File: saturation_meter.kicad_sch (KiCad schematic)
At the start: 18 parts, among them J1 DUT, Q1 Q_NMOS_GDS, Q2 Q_NMOS_GDS, U1 OP07, U2 IR2112

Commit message: Added cap
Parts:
- removed R4: 30k, symbol Device:R
- removed R5: 100k, symbol Device:R
- removed U1: OP07, symbol Amplifier_Operational:OP07
- added C10, C9: 100n, symbol Device:C
- added C11, C12, C13, C4: 4700u, symbol Device:C_Polarized_US
- added C5, C6, C7, C8: 1n, symbol Device:C
- added D4: D, symbol Device:D
- added J2: DUT, symbol Connector_Generic:Conn_01x02
- added R10: 1, symbol Device:R
- added R11, R8: 10k, symbol Device:R
- added R12, R9: 1k, symbol Device:R
- added U1: LM7812_TO220, Package_TO_SOT_THT:TO-220-3_Vertical, symbol Regulator_Linear:LM7812_TO220
- Q1, Q2: value Q_NMOS_GDS -> BUK556
- R2: value 100k -> 1k
- R3: value 30k -> 1k
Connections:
- net GND: now also R3.2, C10.2, C11.2, C12.2, C13.2, C4.2, C5.2, C6.2, C7.2, C8.2, C9.2, J2.1 (Pin_1), R12.1, R9.1, U1.2 (GND)
- net high_nmos_s: now also R8.2
- net low_nmos_g: now also R2.2; no longer R3.1
- net driver_ho: now reaches R6.1, U2.7 (HO)
- net driver_ho: now also R7.1
- net low_nmos_d: now reaches D2.2 (A), J1.2 (Pin_2), Q1.2 (D)
- net low_nmos_d: now also R11.2
- net driver_lo: now reaches U2.1 (LO)
- net driver_lo: no longer R7.1
- net +12V: now reaches C2.1, D3.2 (A), U2.3 (VCC)
- net +12V: now also C10.1, U1.3 (VO)
- net i_sense_high: now reaches R2.1
- net i_sense_high: now also C8.1; no longer R3.2
- net vbus: now reaches D2.1 (K), Q2.2 (D)
- net vbus: now also C11.1, C12.1, C13.1, C4.1, C9.1, R10.2, U1.1 (VI)
- new net: D4.1 (K), R10.1
- new net: D4.2 (A), J2.2 (Pin_2)
- new net dut_high: C5.1, R8.1, R9.2
- new net dut_low: C6.1, R11.1, R12.2
- new net i_sense_low: C7.1, R3.1
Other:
- moved on the sheet: C1, C2, C3, D1, D2, D3, J1, Q1, Q2, R1, R6, R7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

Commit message: Released 1.0.0 of schematic
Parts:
- removed C1, C10, C2: 100n, symbol Device:C
- removed D1, D2, D4: D, symbol Device:D
- removed U1: LM7812_TO220, Package_TO_SOT_THT:TO-220-3_Vertical, symbol Regulator_Linear:LM7812_TO220
- added C12, C13, C9: 2u2, Capacitor_THT:CP_Radial_D6.3mm_P2.50mm, symbol Device:C_Polarized_US
- added D1, D2, D3: 1N5822, Diode_THT:D_DO-201AD_P15.24mm_Horizontal, symbol Diode:1N5822
- added D5, D6: LED, LED_THT:LED_D5.0mm, symbol Device:LED
- added J3: Inputs, Connector_PinHeader_2.54mm:PinHeader_1x03_P2.54mm_Vertical, symbol Connector_Generic:Conn_01x03
- added J4: Outputs, Connector_PinHeader_2.54mm:PinHeader_1x04_P2.54mm_Vertical, symbol Connector_Generic:Conn_01x04
- added J5: UC, Connector_PinHeader_2.54mm:PinHeader_1x02_P2.54mm_Vertical, symbol Connector_Generic:Conn_01x02
- added Q3: BC328, Package_TO_SOT_THT:TO-92_Inline, symbol Transistor_BJT:BC328
- added R11, R14: 1k6, Resistor_SMD:R_1206_3216Metric_Pad1.30x1.75mm_HandSolder, symbol Device:R
- added R12, R17, R18, R19: 8k2, Resistor_SMD:R_1206_3216Metric_Pad1.30x1.75mm_HandSolder, symbol Device:R
- added R13, R15, R16: 100, Resistor_SMD:R_1206_3216Metric_Pad1.30x1.75mm_HandSolder, symbol Device:R
- added U1: LF33_TO220, Package_TO_SOT_THT:TO-220-3_Vertical, symbol Regulator_Linear:LF33_TO220
- C1: renamed from C4; footprint (none) -> Capacitor_THT:CP_Radial_D30.0mm_P10.00mm_SnapIn
- C10: renamed from C7; footprint (none) -> Capacitor_SMD:C_1206_3216Metric_Pad1.33x1.80mm_HandSolder
- C11: renamed from C3; footprint (none) -> Capacitor_SMD:C_1206_3216Metric_Pad1.33x1.80mm_HandSolder
- C2: renamed from C11; footprint (none) -> Capacitor_THT:CP_Radial_D30.0mm_P10.00mm_SnapIn
- C3: renamed from C12; footprint (none) -> Capacitor_THT:CP_Radial_D30.0mm_P10.00mm_SnapIn
- C4: renamed from C13; footprint (none) -> Capacitor_THT:CP_Radial_D30.0mm_P10.00mm_SnapIn
- C5: renamed from C6; footprint (none) -> Capacitor_SMD:C_1206_3216Metric_Pad1.33x1.80mm_HandSolder
- C6: renamed from C5; footprint (none) -> Capacitor_SMD:C_1206_3216Metric_Pad1.33x1.80mm_HandSolder
- C7: renamed from C8; footprint (none) -> Capacitor_SMD:C_1206_3216Metric_Pad1.33x1.80mm_HandSolder
- C8: renamed from C9; footprint (none) -> Capacitor_SMD:C_1206_3216Metric_Pad1.33x1.80mm_HandSolder
- D4: renamed from D3; value D -> 1N4007; footprint (none) -> Diode_THT:D_DO-41_SOD81_P10.16mm_Horizontal; symbol Device:D -> Diode:1N4007
- J1: renamed from J2; value DUT -> Vin; footprint (none) -> TerminalBlock:TerminalBlock_MaiXu_MX126-5.0-02P_1x02_P5.00mm
- J2: renamed from J1; footprint (none) -> Connector:Banana_Jack_2Pin
- Q1: renamed from Q2; footprint (none) -> Package_TO_SOT_THT:TO-220-3_Vertical
- Q2: renamed from Q1; footprint (none) -> Package_TO_SOT_THT:TO-220-3_Vertical
- R1: renamed from R10; value 1 -> 10; footprint (none) -> Resistor_THT:R_Axial_DIN0617_L17.0mm_D6.0mm_P20.32mm_Horizontal
- R10: renamed from R3; footprint (none) -> Resistor_SMD:R_1206_3216Metric_Pad1.30x1.75mm_HandSolder
- R2: renamed from R6; footprint (none) -> Resistor_SMD:R_1206_3216Metric_Pad1.30x1.75mm_HandSolder
- R3: renamed from R8; value 10k -> 8k2; footprint (none) -> Resistor_SMD:R_1206_3216Metric_Pad1.30x1.75mm_HandSolder
- R4: renamed from R11; value 10k -> 8k2; footprint (none) -> Resistor_SMD:R_1206_3216Metric_Pad1.30x1.75mm_HandSolder
- R5: renamed from R9; value 1k -> 1k6; footprint (none) -> Resistor_SMD:R_1206_3216Metric_Pad1.30x1.75mm_HandSolder
- R6: renamed from R12; value 1k -> 1k6; footprint (none) -> Resistor_SMD:R_1206_3216Metric_Pad1.30x1.75mm_HandSolder
- R7: footprint (none) -> Resistor_SMD:R_1206_3216Metric_Pad1.30x1.75mm_HandSolder
- R8: renamed from R2; footprint (none) -> Resistor_SMD:R_1206_3216Metric_Pad1.30x1.75mm_HandSolder
- R9: renamed from R1; footprint (none) -> Resistor_THT:R_Axial_DIN0617_L17.0mm_D6.0mm_P20.32mm_Horizontal
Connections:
- net +12V is gone; now on net vbus: D4.2 (A), U2.3 (VCC)
- net GND: now also C9.2, D3.2 (A), D5.1 (K), D6.1 (K), J5.2 (Pin_2), R17.1, R18.1, R19.1, U1.2 (GND)
- net dut_high: now also C5.1, J4.3 (Pin_3); no longer C6.1
- net dut_low: now also C6.1, J4.4 (Pin_4); no longer C5.1
- net high_nmos_s: now also C12.2, D3.1 (K)
- net i_sense_high: now also J4.1 (Pin_1)
- net i_sense_low: now also J4.2 (Pin_2)
- net low_nmos_d: now also D2.2 (A)
- net low_nmos_s: now also C13.2
- net vbus: now also C13.1, D2.1 (K), R11.2, R12.2, U1.1 (VI)
- net charge_det: now reaches R1.1
- net charge_det: now also D1.1 (K), Q3.3 (E)
- net vin: now reaches J1.2 (Pin_2)
- net vin: now also D1.2 (A)
- net at U2.10 (HIN): now also R13.2
- net at U2.11 (SD): now also R16.2
- net at U2.12 (LIN): now also R15.2
- net at D4.1 (K), U2.6 (VB): now also C12.1
- net +3.3V: now reaches C11.1, U2.9 (VDD)
- net +3.3V: now also C9.1, J5.1 (Pin_1), U1.3 (VO)
- new net: Q3.2 (B), R12.1
- new net: D6.2 (A), R14.1
- new net: Q3.1 (C), R14.2
- new net: D5.2 (A), R11.1
- new net hin_uc: J3.1 (Pin_1), R13.1, R17.2
- new net lin_uc: J3.2 (Pin_2), R15.1, R18.2
- new net sd_uc: J3.3 (Pin_3), R16.1, R19.2
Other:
- title: (none) -> Saturation Meter
- moved on the sheet: C11, C5, C6, C8, D4, R1, U2

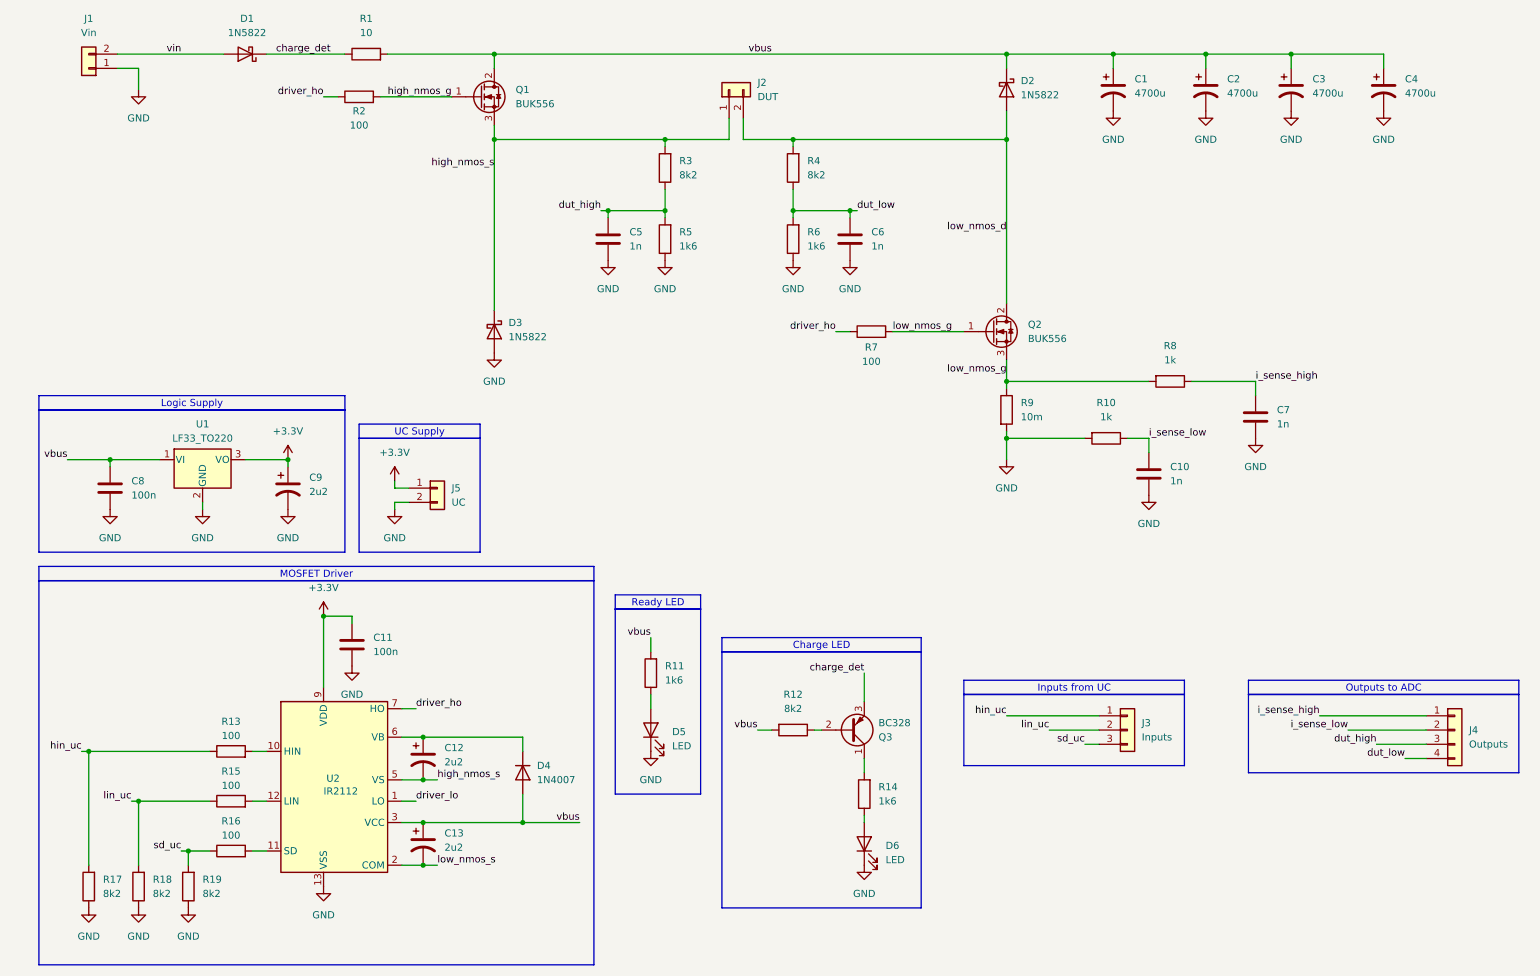
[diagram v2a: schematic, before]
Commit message: First version of PCB, ready to isolation milling
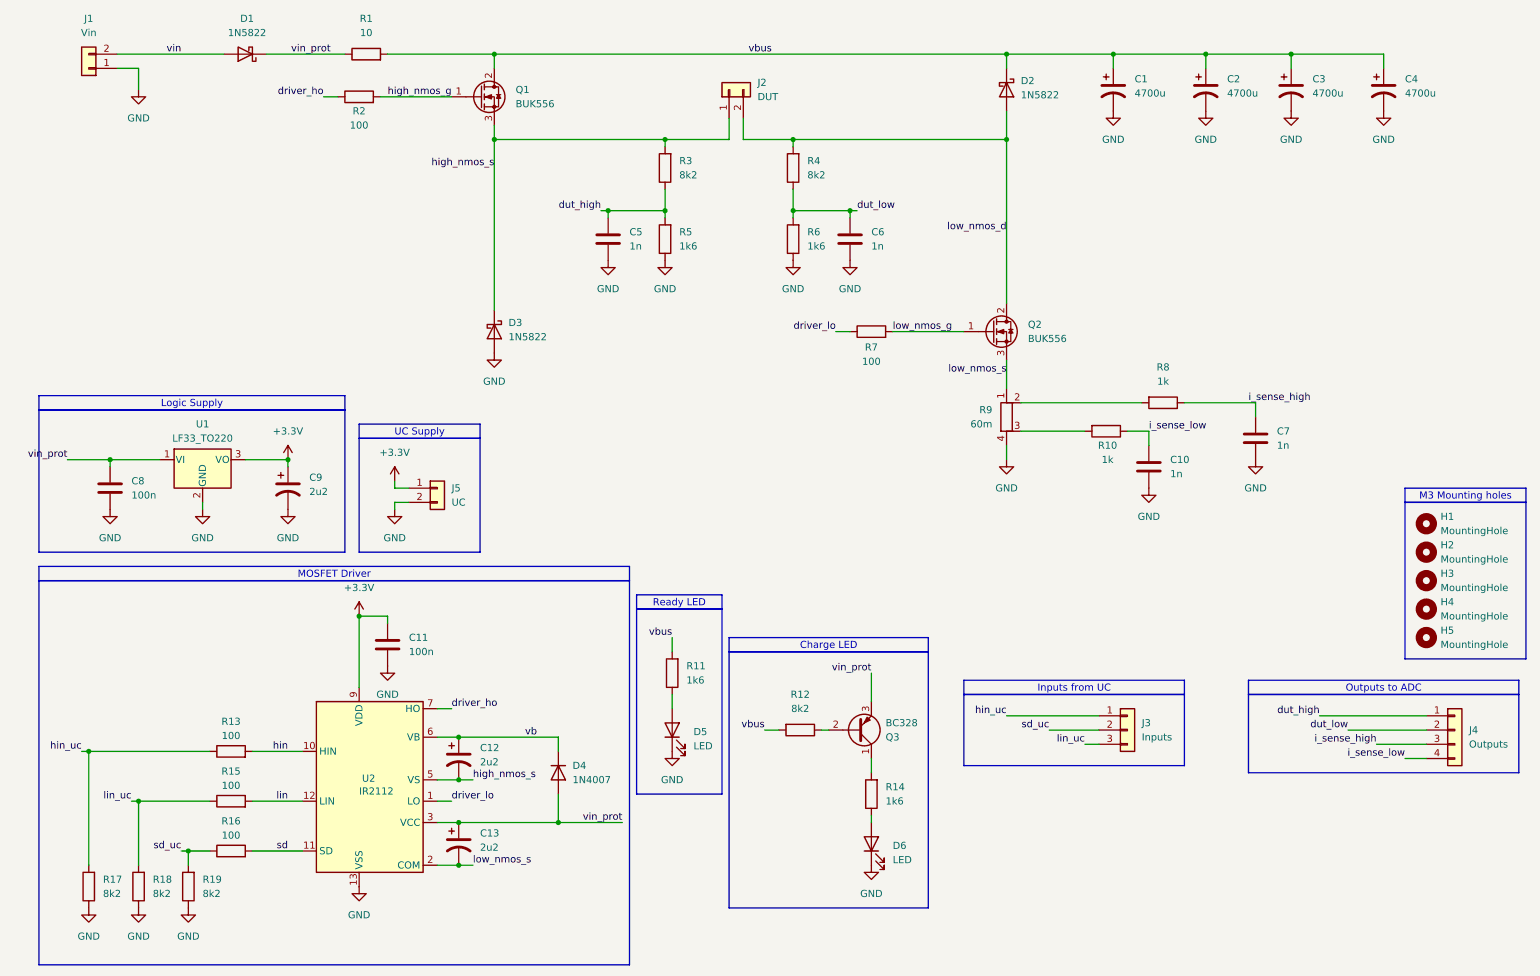
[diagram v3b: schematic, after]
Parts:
- removed R9: 10m, Resistor_THT:R_Axial_DIN0617_L17.0mm_D6.0mm_P20.32mm_Horizontal, symbol Device:R
- added H1, H2, H3, H4, H5: MountingHole, MountingHole:MountingHole_3.2mm_M3_DIN965, symbol Mechanical:MountingHole
- added R9: 60m, shunt:R_Shunt_kelvin_60mohm, symbol Device:R_Shunt
- C10, C11, C5, C6, C7, C8: footprint Capacitor_SMD:C_1206_3216Metric_Pad1.33x1.80mm_HandSolder -> Capacitor_THT:C_Disc_D6.0mm_W2.5mm_P5.00mm
- R10, R11, R12, R13, R14, R15, R16, R17, R18, R19, R2, R3, R4, R5, R6, R7, R8: footprint Resistor_SMD:R_1206_3216Metric_Pad1.30x1.75mm_HandSolder -> Resistor_THT:R_Axial_DIN0207_L6.3mm_D2.5mm_P10.16mm_Horizontal
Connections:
- net GND: now also R9.4; no longer R10.2
- net driver_ho: no longer R7.1
- net driver_lo: now also R7.1
- net dut_high: now also J4.1 (Pin_1); no longer J4.3 (Pin_3)
- net dut_low: now also J4.2 (Pin_2); no longer J4.4 (Pin_4)
- net i_sense_high: now also J4.3 (Pin_3); no longer J4.1 (Pin_1)
- net i_sense_low: now also J4.4 (Pin_4); no longer J4.2 (Pin_2)
- net lin_uc: now also J3.3 (Pin_3); no longer J3.2 (Pin_2)
- net low_nmos_g: no longer Q2.3 (S), R8.2
- net low_nmos_s: now also Q2.3 (S), R9.1
- net sd_uc: now also J3.2 (Pin_2); no longer J3.3 (Pin_3)
- net vbus: no longer C13.1, C8.1, D4.2 (A), U1.1 (VI), U2.3 (VCC)
- net sd: now reaches R16.2, U2.11 (SD)
- net lin: now reaches R15.2, U2.12 (LIN)
- net hin: now reaches R13.2, U2.10 (HIN)
- net vb: now reaches C12.1, D4.1 (K), U2.6 (VB)
- net charge_det renamed vin_prot
- net vin_prot: now also C13.1, C8.1, D4.2 (A), U1.1 (VI), U2.3 (VCC)
- new net: R8.2, R9.2
- new net: R10.2, R9.3
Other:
- moved on the sheet: C10, C11, C12, C13, C7, D4, D5, D6, Q3, R10, R11, R12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

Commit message: Updated to double layer
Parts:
- added R20: 100k, Resistor_THT:R_Axial_DIN0207_L6.3mm_D2.5mm_P10.16mm_Horizontal, symbol Device:R
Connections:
- net GND: now also R20.1
- net vbus: now also R20.2
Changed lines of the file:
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@@
+	)
+	(junction
+		(at 256.54 34.29)
+		(diameter 0)
+		(color 0 0 0 0)
 	)
 	(junction
@@
 	(wire
 		(pts
+			(xy 271.78 34.29) (xy 256.54 34.29)
+		)
+		(stroke
+			(width 0)
+			(type default)
+		)
+	)
+	(wire
+		(pts
 			(xy 87.63 156.21) (xy 91.44 156.21)
 		)
@@
 		(pts
 			(xy 156.21 154.94) (xy 157.48 154.94)
+		)
+		(stroke
+			(width 0)
+			(type default)
+		)
+	)
+	(wire
+		(pts
+			(xy 271.78 36.83) (xy 271.78 34.29)
 		)
 		(stroke
@@
 	(symbol
 		(lib_id "power:GND")
+		(at 271.78 44.45 0)
+		(unit 1)
+		(exclude_from_sim no)
+		(in_bom yes)
+		(on_board yes)
+		(dnp no)
+		(fields_autoplaced yes)
+		(property "Reference" "#PWR028"
+			(at 271.78 50.8 0)
+			(effects
+				(font
+					(size 1.27 1.27)
+				)
+				(hide yes)
+			)
+		)
+		(property "Value" "GND"
+			(at 271.78 49.53 0)
+			(effects
+				(font
+					(size 1.27 1.27)
+				)
+			)
+		)
+		(property "Footprint" ""
+			(at 271.78 44.45 0)
+			(effects
+				(font
+					(size 1.27 1.27)
+				)
+				(hide yes)
+			)
+		)
+		(property "Datasheet" ""
+			(at 271.78 44.45 0)
+			(effects
+				(font
+					(size 1.27 1.27)
+				)
+				(hide yes)
+			)
+		)
+		(property "Description" "Power symbol creates a global label with name \"GND\" , ground"
+			(at 271.78 44.45 0)
+			(effects
+				(font
+					(size 1.27 1.27)
+				)
+				(hide yes)
+			)
+		)
+		(pin "1"
+		)
+		(instances
+			(project "saturation_meter"
+				(path "/26524b93-4c12-433d-9334-06c7258f4cea"
+					(reference "#PWR028")
+					(unit 1)
+				)
+			)
+		)
+	)
+	(symbol
+		(lib_id "power:GND")
 		(at 256.54 44.45 0)
 		(unit 1)
@@
 					(unit 1)
 				)
+			)
+		)
+	)
+	(symbol
+		(lib_id "Device:R")
+		(at 271.78 40.64 180)
+		(unit 1)
+		(exclude_from_sim no)
+		(in_bom yes)
+		(on_board yes)
+		(dnp no)
+		(fields_autoplaced yes)
+		(property "Reference" "R20"
+			(at 274.32 39.3699 0)
+			(effects
+				(font
+					(size 1.27 1.27)
+				)
+				(justify right)
+			)
+		)
+		(property "Value" "100k"
+			(at 274.32 41.9099 0)
+			(effects
+				(font
+					(size 1.27 1.27)
+				)
+				(justify right)
+			)
+		)
+		(property "Footprint" "Resistor_THT:R_Axial_DIN0207_L6.3mm_D2.5mm_P10.16mm_Horizontal"
+			(at 273.558 40.64 90)
+			(effects
+				(font
+					(size 1.27 1.27)
+				)
+				(hide yes)
+			)
+		)
+		(property "Datasheet" "~"
+			(at 271.78 40.64 0)
+			(effects
+				(font
+					(size 1.27 1.27)
+				)
+				(hide yes)
+			)
+		)
+		(property "Description" "Resistor"
+			(at 271.78 40.64 0)
+			(effects
+				(font
+					(size 1.27 1.27)
+				)
+				(hide yes)
+			)
+		)
+		(pin "1"
+		)
+		(pin "2"
+		)
+		(instances
+			(project "saturation_meter"
+				(path "/26524b93-4c12-433d-9334-06c7258f4cea"
+					(reference "R20")
+					(unit 1)
+				)

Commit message: Updated to v1.1.0 fixed, shutdown of ir2112, added enclosure
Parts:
- removed Q3: BC328, Package_TO_SOT_THT:TO-92_Inline, symbol Transistor_BJT:BC328
- added D7: 1N4007, Diode_THT:D_DO-41_SOD81_P10.16mm_Horizontal, symbol Diode:1N4007
- added Q4: BC638, Package_TO_SOT_THT:TO-92_Inline, symbol Transistor_BJT:BC636
- R20: value 100k -> 8k2
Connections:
- net +3.3V: now also R19.2, D7.2 (A)
- net GND: no longer R19.1
- net hin_uc: now also J3.2 (Pin_2); no longer J3.1 (Pin_1)
- net sd_uc: now also J3.1 (Pin_1), R19.1; no longer J3.2 (Pin_2), R19.2
- net vin_prot: now also D7.1 (K), Q4.1 (E)
- net at R12.1: now also Q4.3 (B)
- net at R14.2: now also Q4.2 (C)
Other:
- moved on the sheet: C11, C12, C13, C8, C9, D4, J5, R13, R15, R16, R17, R18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
